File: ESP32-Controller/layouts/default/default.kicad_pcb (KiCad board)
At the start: 2 copper layers, 62 x 30 mm, 41 parts

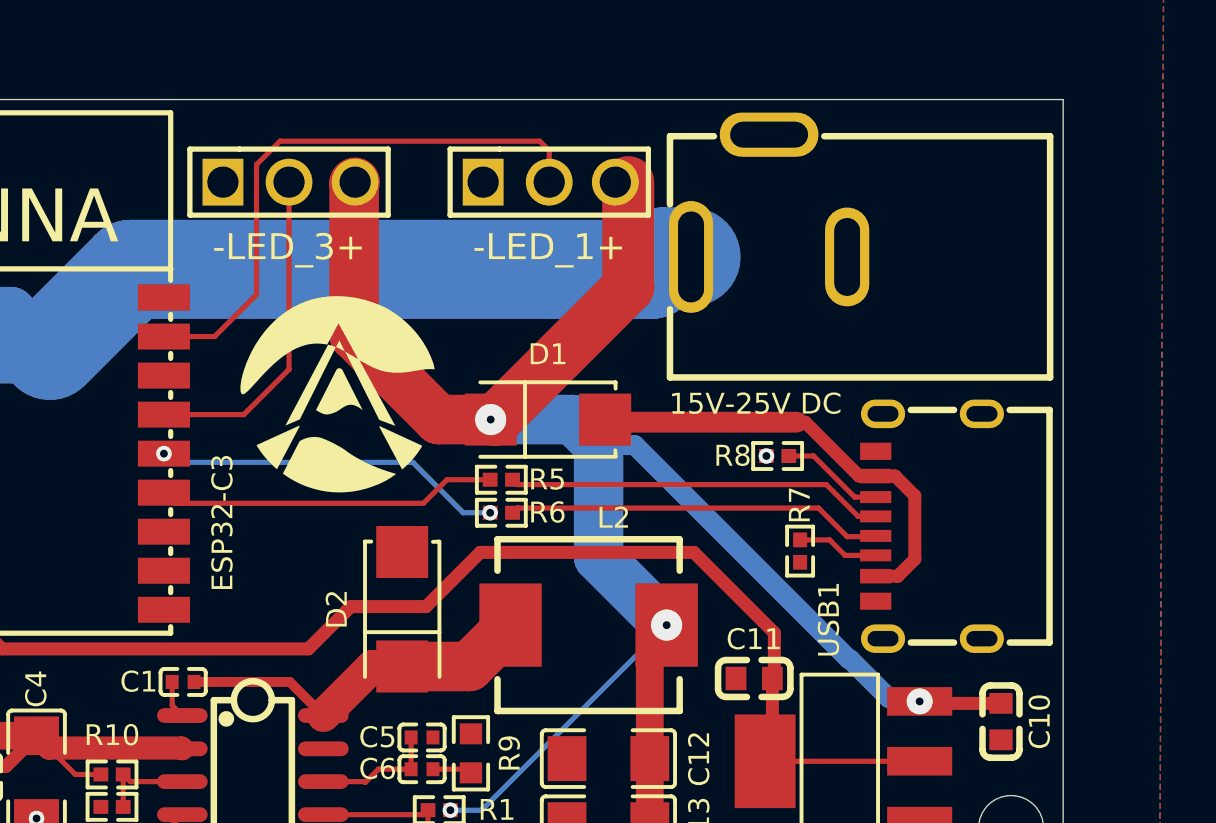
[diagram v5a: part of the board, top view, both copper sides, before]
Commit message: Fixed USB port
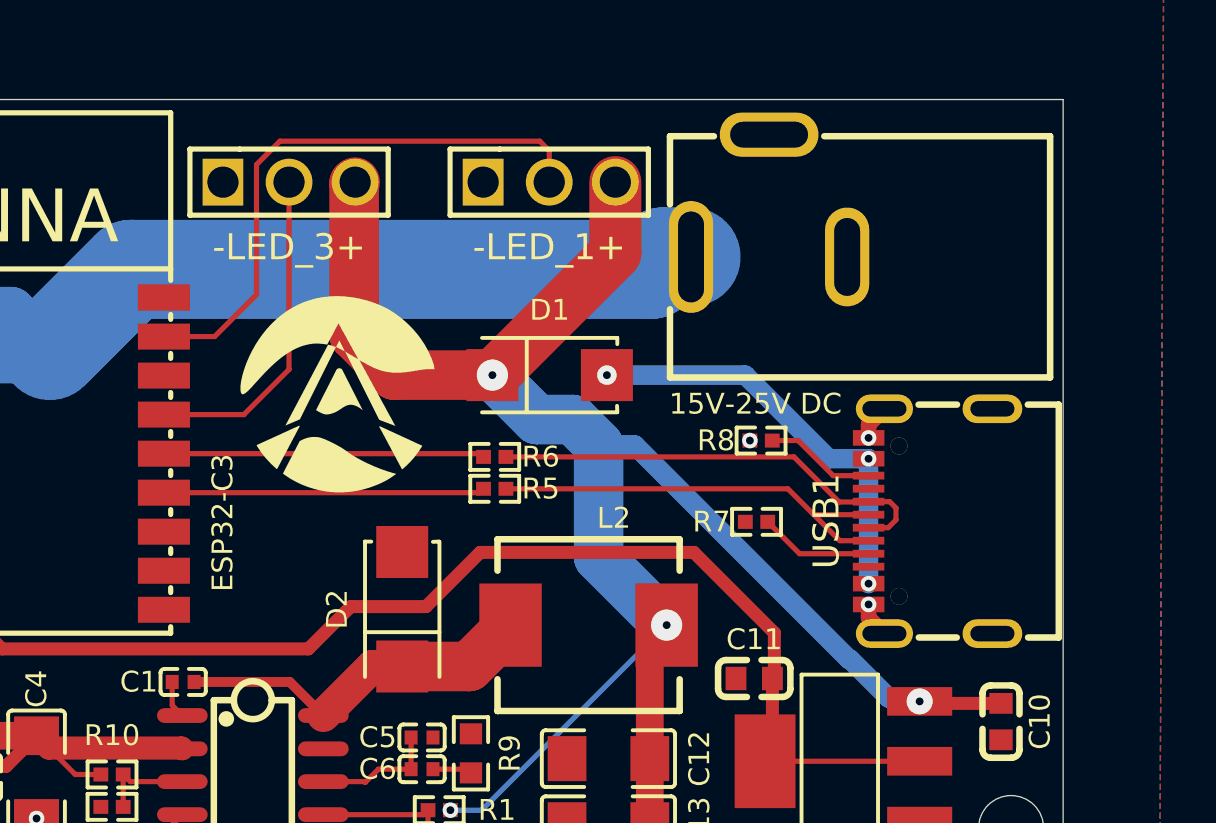
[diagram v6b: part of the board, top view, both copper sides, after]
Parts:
- USB1: footprint Hanbo_Electronic_MC_403L68_Z20:USB-C-SMD_MC-403L68-Z20 -> BXCONN_UC09_0B16F00P11:USB-C_UC09-0B16F00P11
- moved REF** 14.3 mm to (136.4, 118.8)
- moved QR***** 10.6 mm to (148.5, 115.8)
- moved REF** 10.5 mm to (136.4, 111.7)
- moved R6 2.16 mm to (140.2, 113.7)
- moved R7 2.02 mm to (150.2, 116.2), turned to 180 degrees
- moved D1 1.71 mm to (142.3, 110.6)
- moved R8 0.87 mm to (150.4, 113.1)
- moved R5 0.43 mm to (140.2, 115.0)
- moved USB1 0.21 mm to (156.9, 116.2)
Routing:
- net usb_p: track 14.5 -> 17.4 mm
- net GND: track 0.00 -> 2.74 mm, vias 12 -> 14
- net usb_n: track 14.5 -> 17.0 mm
- net 5V: track 74.4 -> 72.3 mm
- net 14: track 13.7 -> 12.3 mm, vias 2 -> 0
- net CC1: track 3.33 -> 4.38 mm
- net vUSB: track 17.2 -> 16.2 mm, vias 0 -> 3
- net 13: track 13.1 -> 12.3 mm
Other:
- board text added: "ESP32 LED Panel Controller v1.1.2 - June 2026"
- board text removed: "ESP32 LED Panel Controller v1.1.1 - June 2026"
